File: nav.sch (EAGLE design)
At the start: 61 parts, among them IC1 FT230XQ, SW1 DHT-4235A, U2 ATMEGA2560-16AU100A-M, U3 MPL3115A2, Y1 16MHz

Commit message: Added Barometer
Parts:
- added C3: 10u, resistor:C-EUC0603
- added C4, C5: 100n, resistor:C-EUC0603
- added R14, R20: (no value), resistor:R-EU_R0603
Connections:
- new net BARO_INT1: U2A.PK0_(ADC8/PCINT16), U3.INT1
- new net BARO_INT2: U2A.PK1_(ADC9/PCINT17), U3.INT2
- new net N$17: C5.1, U3.CAP
- new net SCL: R14.1, U2A.(SCL/INT0)_PD0, U3.SCL
- new net SDA: R20.1, U2A.(SDA/INT1)_PD1, U3.SDA
- net +3V3: now also C3.1, C4.1, R14.2, R20.2, U3.VDD, U3.VDDIO
- net GND: now also C3.2, C4.2, C5.2, U3.GND
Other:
- moved on the sheet: U3
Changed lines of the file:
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@@
 <part name="+3V3" library="supply1" library_urn="urn:adsk.eagle:library:371" deviceset="+3V3" device=""/>
 <part name="GND12" library="supply1" library_urn="urn:adsk.eagle:library:371" deviceset="GND" device=""/>
+<part name="+3V4" library="supply1" library_urn="urn:adsk.eagle:library:371" deviceset="+3V3" device=""/>
+<part name="C3" library="resistor" library_urn="urn:adsk.eagle:library:348" deviceset="C-EU" device="C0603" package3d_urn="urn:adsk.eagle:package:23616/2" value="10u"/>
+<part name="C4" library="resistor" library_urn="urn:adsk.eagle:library:348" deviceset="C-EU" device="C0603" package3d_urn="urn:adsk.eagle:package:23616/2" value="100n"/>
+<part name="C5" library="resistor" library_urn="urn:adsk.eagle:library:348" deviceset="C-EU" device="C0603" package3d_urn="urn:adsk.eagle:package:23616/2" value="100n"/>
+<part name="GND14" library="supply1" library_urn="urn:adsk.eagle:library:371" deviceset="GND" device=""/>
+<part name="+3V5" library="supply1" library_urn="urn:adsk.eagle:library:371" deviceset="+3V3" device=""/>
+<part name="GND15" library="supply1" library_urn="urn:adsk.eagle:library:371" deviceset="GND" device=""/>
+<part name="R14" library="resistor" library_urn="urn:adsk.eagle:library:348" deviceset="R-EU_" device="R0603" package3d_urn="urn:adsk.eagle:package:23555/2"/>
+<part name="R20" library="resistor" library_urn="urn:adsk.eagle:library:348" deviceset="R-EU_" device="R0603" package3d_urn="urn:adsk.eagle:package:23555/2"/>
+<part name="+3V7" library="supply1" library_urn="urn:adsk.eagle:library:371" deviceset="+3V3" device=""/>
 </parts>
 <sheets>
@@
 <instance part="GND5" gate="1" x="200.66" y="76.2"/>
 <instance part="FRAME3" gate="G$1" x="0" y="0"/>
+<instance part="R14" gate="G$1" x="27.94" y="68.58" rot="R90"/>
+<instance part="R20" gate="G$1" x="33.02" y="66.04" rot="R90"/>
+<instance part="+3V7" gate="G$1" x="22.86" y="76.2" rot="R90"/>
 </instances>
 <busses>
@@
 <junction x="195.58" y="149.86"/>
 </segment>
+<segment>
+<pinref part="R20" gate="G$1" pin="2"/>
+<wire x1="33.02" y1="71.12" x2="33.02" y2="76.2" width="0.1524" layer="91"/>
+<pinref part="R14" gate="G$1" pin="2"/>
+<wire x1="33.02" y1="76.2" x2="27.94" y2="76.2" width="0.1524" layer="91"/>
+<wire x1="27.94" y1="76.2" x2="27.94" y2="73.66" width="0.1524" layer="91"/>
+<wire x1="27.94" y1="76.2" x2="25.4" y2="76.2" width="0.1524" layer="91"/>
+<junction x="27.94" y="76.2"/>
+<pinref part="+3V7" gate="G$1" pin="+3V3"/>
+</segment>
 </net>
 <net name="GPS_TX" class="0">
@@
 <wire x1="50.8" y1="50.8" x2="45.72" y2="50.8" width="0.1524" layer="91"/>
 <label x="45.72" y="50.8" size="1.778" layer="95" rot="R180" xref="yes"/>
+</segment>
+</net>
+<net name="SDA" class="0">
+<segment>
+<pinref part="U2" gate="A" pin="(SDA/INT1)_PD1"/>
+<wire x1="50.8" y1="60.96" x2="33.02" y2="60.96" width="0.1524" layer="91"/>
+<pinref part="R20" gate="G$1" pin="1"/>
+<wire x1="33.02" y1="60.96" x2="22.86" y2="60.96" width="0.1524" layer="91"/>
+<junction x="33.02" y="60.96"/>
+<label x="22.86" y="60.96" size="1.778" layer="95" rot="R180" xref="yes"/>
+</segment>
+</net>
+<net name="SCL" class="0">
+<segment>
+<pinref part="U2" gate="A" pin="(SCL/INT0)_PD0"/>
+<wire x1="50.8" y1="63.5" x2="27.94" y2="63.5" width="0.1524" layer="91"/>
+<pinref part="R14" gate="G$1" pin="1"/>
+<wire x1="27.94" y1="63.5" x2="22.86" y2="63.5" width="0.1524" layer="91"/>
+<junction x="27.94" y="63.5"/>
+<label x="22.86" y="63.5" size="1.778" layer="95" rot="R180" xref="yes"/>
+</segment>
+</net>
+<net name="BARO_INT1" class="0">
+<segment>
+<pinref part="U2" gate="A" pin="PK0_(ADC8/PCINT16)"/>
+<wire x1="157.48" y1="127" x2="160.02" y2="127" width="0.1524" layer="91"/>
+<label x="160.02" y="127" size="1.778" layer="95" xref="yes"/>
+</segment>
+</net>
+<net name="BARO_INT2" class="0">
+<segment>
+<pinref part="U2" gate="A" pin="PK1_(ADC9/PCINT17)"/>
+<wire x1="157.48" y1="124.46" x2="160.02" y2="124.46" width="0.1524" layer="91"/>
+<label x="160.02" y="124.46" size="1.778" layer="95" xref="yes"/>
 </segment>
 </net>
@@
 <instance part="FRAME4" gate="G$1" x="0" y="0"/>
 <instance part="U1" gate="G$1" x="106.68" y="203.2"/>
-<instance part="U3" gate="G$1" x="266.7" y="213.36"/>
+<instance part="U3" gate="G$1" x="317.5" y="193.04"/>
 <instance part="+3V1" gate="G$1" x="86.36" y="228.6"/>
 <instance part="GND2" gate="1" x="83.82" y="208.28" rot="R270"/>
@@
 <instance part="+3V3" gate="G$1" x="187.96" y="198.12"/>
 <instance part="GND12" gate="1" x="187.96" y="175.26"/>
+<instance part="+3V4" gate="G$1" x="294.64" y="205.74"/>
+<instance part="C3" gate="G$1" x="276.86" y="193.04"/>
+<instance part="C4" gate="G$1" x="266.7" y="193.04"/>
+<instance part="C5" gate="G$1" x="287.02" y="190.5"/>
+<instance part="GND14" gate="1" x="292.1" y="175.26"/>
+<instance part="+3V5" gate="G$1" x="271.78" y="203.2"/>
+<instance part="GND15" gate="1" x="271.78" y="180.34"/>
 </instances>
 <busses>
@@
 <junction x="187.96" y="193.04"/>
 <pinref part="+3V3" gate="G$1" pin="+3V3"/>
+</segment>
+<segment>
+<pinref part="U3" gate="G$1" pin="VDD"/>
+<wire x1="304.8" y1="195.58" x2="294.64" y2="195.58" width="0.1524" layer="91"/>
+<wire x1="294.64" y1="195.58" x2="294.64" y2="203.2" width="0.1524" layer="91"/>
+<pinref part="U3" gate="G$1" pin="VDDIO"/>
+<wire x1="304.8" y1="187.96" x2="294.64" y2="187.96" width="0.1524" layer="91"/>
+<wire x1="294.64" y1="187.96" x2="294.64" y2="195.58" width="0.1524" layer="91"/>
+<junction x="294.64" y="195.58"/>
+<pinref part="+3V4" gate="G$1" pin="+3V3"/>
+</segment>
+<segment>
+<pinref part="C4" gate="G$1" pin="1"/>
+<wire x1="266.7" y1="195.58" x2="266.7" y2="198.12" width="0.1524" layer="91"/>
+<pinref part="C3" gate="G$1" pin="1"/>
+<wire x1="266.7" y1="198.12" x2="271.78" y2="198.12" width="0.1524" layer="91"/>
+<wire x1="271.78" y1="198.12" x2="276.86" y2="198.12" width="0.1524" layer="91"/>
+<wire x1="276.86" y1="198.12" x2="276.86" y2="195.58" width="0.1524" layer="91"/>
+<wire x1="271.78" y1="198.12" x2="271.78" y2="200.66" width="0.1524" layer="91"/>
+<junction x="271.78" y="198.12"/>
+<pinref part="+3V5" gate="G$1" pin="+3V3"/>
 </segment>
 </net>
@@
 <pinref part="GND12" gate="1" pin="GND"/>
 </segment>
+<segment>
+<pinref part="U3" gate="G$1" pin="GND"/>
+<wire x1="304.8" y1="190.5" x2="297.18" y2="190.5" width="0.1524" layer="91"/>
+<wire x1="297.18" y1="190.5" x2="297.18" y2="180.34" width="0.1524" layer="91"/>
+<pinref part="C5" gate="G$1" pin="2"/>
+<wire x1="297.18" y1="180.34" x2="292.1" y2="180.34" width="0.1524" layer="91"/>
+<wire x1="292.1" y1="180.34" x2="287.02" y2="180.34" width="0.1524" layer="91"/>
+<wire x1="287.02" y1="180.34" x2="287.02" y2="185.42" width="0.1524" layer="91"/>
+<wire x1="292.1" y1="180.34" x2="292.1" y2="177.8" width="0.1524" layer="91"/>
+<junction x="292.1" y="180.34"/>
+<pinref part="GND14" gate="1" pin="GND"/>
+</segment>
+<segment>
+<pinref part="C3" gate="G$1" pin="2"/>
+<wire x1="276.86" y1="187.96" x2="276.86" y2="185.42" width="0.1524" layer="91"/>
+<wire x1="276.86" y1="185.42" x2="271.78" y2="185.42" width="0.1524" layer="91"/>
+<pinref part="C4" gate="G$1" pin="2"/>
+<wire x1="271.78" y1="185.42" x2="266.7" y2="185.42" width="0.1524" layer="91"/>
+<wire x1="266.7" y1="185.42" x2="266.7" y2="187.96" width="0.1524" layer="91"/>
+<wire x1="271.78" y1="185.42" x2="271.78" y2="182.88" width="0.1524" layer="91"/>
+<junction x="271.78" y="185.42"/>
+<pinref part="GND15" gate="1" pin="GND"/>
+</segment>
 </net>
 <net name="!GPS_RST" class="0">
@@
 </segment>
 </net>
+<net name="N$17" class="0">
+<segment>
+<pinref part="U3" gate="G$1" pin="CAP"/>
+<pinref part="C5" gate="G$1" pin="1"/>
+<wire x1="304.8" y1="193.04" x2="287.02" y2="193.04" width="0.1524" layer="91"/>
+</segment>
+</net>
+<net name="SCL" class="0">
+<segment>
+<pinref part="U3" gate="G$1" pin="SCL"/>
+<wire x1="330.2" y1="195.58" x2="332.74" y2="195.58" width="0.1524" layer="91"/>
+<label x="332.74" y="195.58" size="1.778" layer="95" xref="yes"/>
+</segment>
+</net>
+<net name="SDA" class="0">
+<segment>
+<pinref part="U3" gate="G$1" pin="SDA"/>
+<wire x1="330.2" y1="193.04" x2="332.74" y2="193.04" width="0.1524" layer="91"/>
+<label x="332.74" y="193.04" size="1.778" layer="95" xref="yes"/>
+</segment>
+</net>
+<net name="BARO_INT1" class="0">
+<segment>
+<pinref part="U3" gate="G$1" pin="INT1"/>
+<wire x1="330.2" y1="190.5" x2="332.74" y2="190.5" width="0.1524" layer="91"/>
+<label x="332.74" y="190.5" size="1.778" layer="95" xref="yes"/>
+</segment>
+</net>
+<net name="BARO_INT2" class="0">
+<segment>
+<pinref part="U3" gate="G$1" pin="INT2"/>
+<wire x1="330.2" y1="187.96" x2="332.74" y2="187.96" width="0.1524" layer="91"/>
+<label x="332.74" y="187.96" size="1.778" layer="95" xref="yes"/>
+</segment>
+</net>

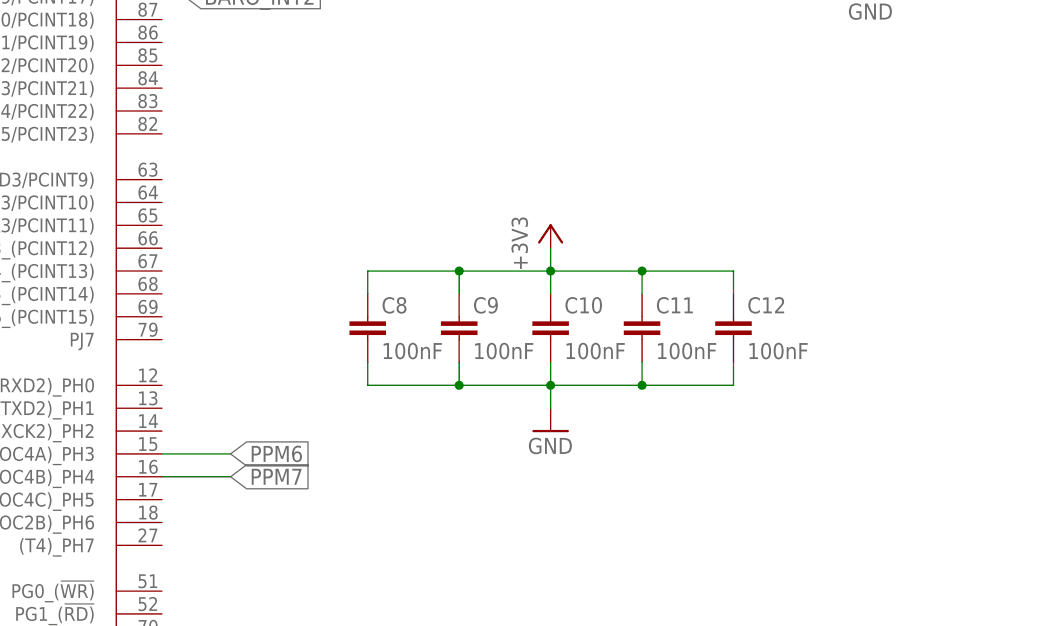
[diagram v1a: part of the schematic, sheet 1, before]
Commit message: Added LoRa
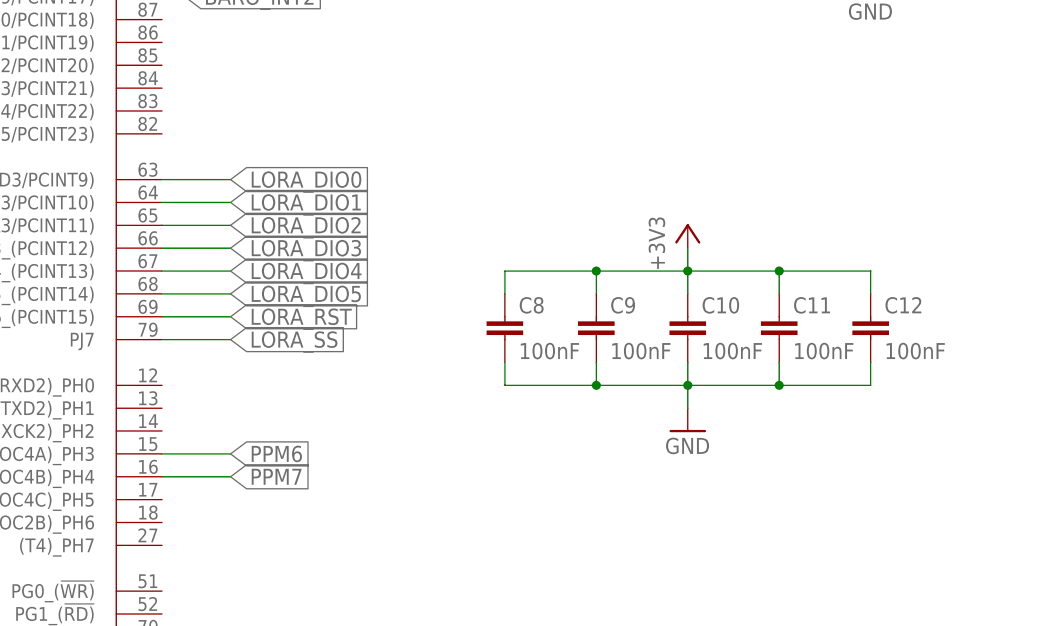
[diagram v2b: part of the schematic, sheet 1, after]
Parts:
- added R21: (no value), resistor:R-EU_R0603
- added U4: 433MHz, SparkFun-RF:RFM69HCW-433
- added X1: (no value), adafruit:SMACONNECTOR_EDGE
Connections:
- new net !LORA_RST: R21.1, U2A.PJ6_(PCINT15), U4.RESET
- new net !LORA_SS: U2A.PJ7, U4.NSS
- new net LORA_DIO0: U2A.PJ0_(RXD3/PCINT9), U4.DIO0
- new net LORA_DIO1: U2A.PJ1_(TXD3/PCINT10), U4.DIO1
- new net LORA_DIO2: U2A.PJ2_(XCK3/PCINT11), U4.DIO2
- new net LORA_DIO3: U2A.PJ3_(PCINT12), U4.DIO3
- new net LORA_DIO4: U2A.PJ4_(PCINT13), U4.DIO4
- new net LORA_DIO5: U2A.PJ5_(PCINT14), U4.DIO5
- new net N$30: U4.ANT, X1.ANT
- net +3V3: now also R21.2, U4.3.3V
- net GND: now also U4.GND@1, U4.GND@2, X1.GND1, X1.GND2, X1.GND3, X1.GND4
- net MISO: now also U4.MISO
- net MOSI: now also U4.MOSI
- net SCK: now also U4.SCK
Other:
- note added: "RFM69 and RFM96W have the same pinout so the same schematic is used."
- moved on the sheet: C10, C11, C12, C8, C9

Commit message: Added Connectors for HC-SR04, UART3 and I2C
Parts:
- added JP2, JP3, JP4, SONAR0, SONAR1: (no value), pinhead:PINHD-1X4
- renumbered X1 to LORA
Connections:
- new net SCL_5V: JP3.3, JP4.3
- new net SDA_5V: JP3.2, JP4.2
- new net SONAR0_ECHO_3V3: U2A.PK4_(ADC12/PCINT20)
- new net SONAR0_ECHO_5V: SONAR0.3
- new net SONAR0_TRIGGER_3V3: U2A.(OC5A)_PL3
- new net SONAR0_TRIGGER_5V: SONAR0.2
- new net SONAR1_ECHO_3V3: U2A.PK5_(ADC13/PCINT21)
- new net SONAR1_ECHO_5V: SONAR1.3
- new net SONAR1_TRIGGER_3V3: U2A.(OC5B)_PL4
- new net SONAR1_TRIGGER_5V: SONAR1.2
- new net UART3_RX_5V: JP2.3
- new net UART3_TX_5V: JP2.2
- net +5V: now also JP2.1, JP3.1, JP4.1, SONAR0.1, SONAR1.1
- net GND: now also JP2.4, JP3.4, JP4.4, SONAR0.4, SONAR1.4
- net LED3: now also U2A.PK2_(ADC10/PCINT18); no longer U2A.(OC5A)_PL3
- net LED4: now also U2A.PK3_(ADC11/PCINT19); no longer U2A.(OC5B)_PL4

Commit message: First draft of the layout finished
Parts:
- removed PPM4, PPM5, PPM6, PPM7: (no value), pinhead:PINHD-1X3
- added R22, R23: 10k, resistor:R-EU_R0603
- added U5, U6: (no value), adafruit:TXB0104PWR
- renumbered JP1 to POWER, JP2 to UART2, JP3 to I2C_0, JP4 to I2C_1, SW1 to RESET
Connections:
- removed net PPM4: PPM4.1, U2A.(OC3B/INT4)_PE4
- removed net PPM5: PPM5.1, U2A.(OC3C/INT5)_PE5
- removed net PPM6: PPM6.1, U2A.(OC4A)_PH3
- removed net PPM7: PPM7.1, U2A.(OC4B)_PH4
- removed net UART3_RX_5V: UART2.3
- removed net UART3_TX_5V: UART2.2
- new net N$36: R23.1, U6.OE
- new net N$37: R22.1, U5.OE
- new net UART2_RX: U2A.(RXD2)_PH0, U5.A1
- new net UART2_RX_5V: U5.B1, UART2.3
- new net UART2_TX: U2A.(TXD2)_PH1, U5.A2
- new net UART2_TX_5V: U5.B2, UART2.2
- net +3V3: now also U5.VCCA, U6.VCCA
- net +5V: now also R22.2, R23.2, U5.VCCB, U6.VCCB; no longer PPM4.2, PPM5.2, PPM6.2, PPM7.2
- net GND: now also U5.GND, U6.GND; no longer PPM4.3, PPM5.3, PPM6.3, PPM7.3
- net SCL: now also U5.A4
- net SCL_5V: now also U5.B4
- net SDA: now also U5.A3
- net SDA_5V: now also U5.B3
- net SONAR0_ECHO_3V3: now also U6.A1
- net SONAR0_ECHO_5V: now also U6.B1
- net SONAR0_TRIGGER_3V3: now also U6.A2
- net SONAR0_TRIGGER_5V: now also U6.B2
- net SONAR1_ECHO_3V3: now also U6.A3
- net SONAR1_ECHO_5V: now also U6.B3
- net SONAR1_TRIGGER_3V3: now also U6.A4
- net SONAR1_TRIGGER_5V: now also U6.B4
